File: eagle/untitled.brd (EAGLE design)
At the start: 100 x 80 mm, 11 parts, among them U1 ESP-WROOM-32

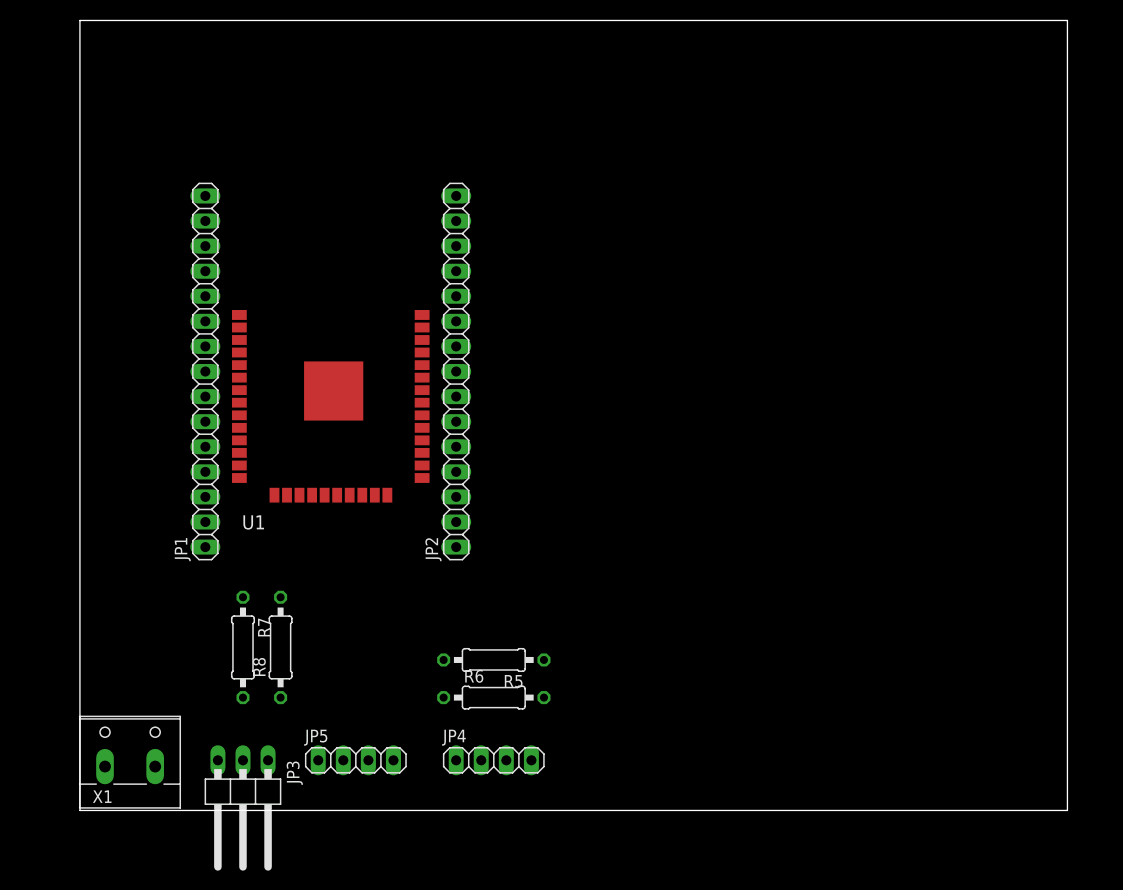
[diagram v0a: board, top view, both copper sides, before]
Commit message: #Eagle - Change Arduino symbol
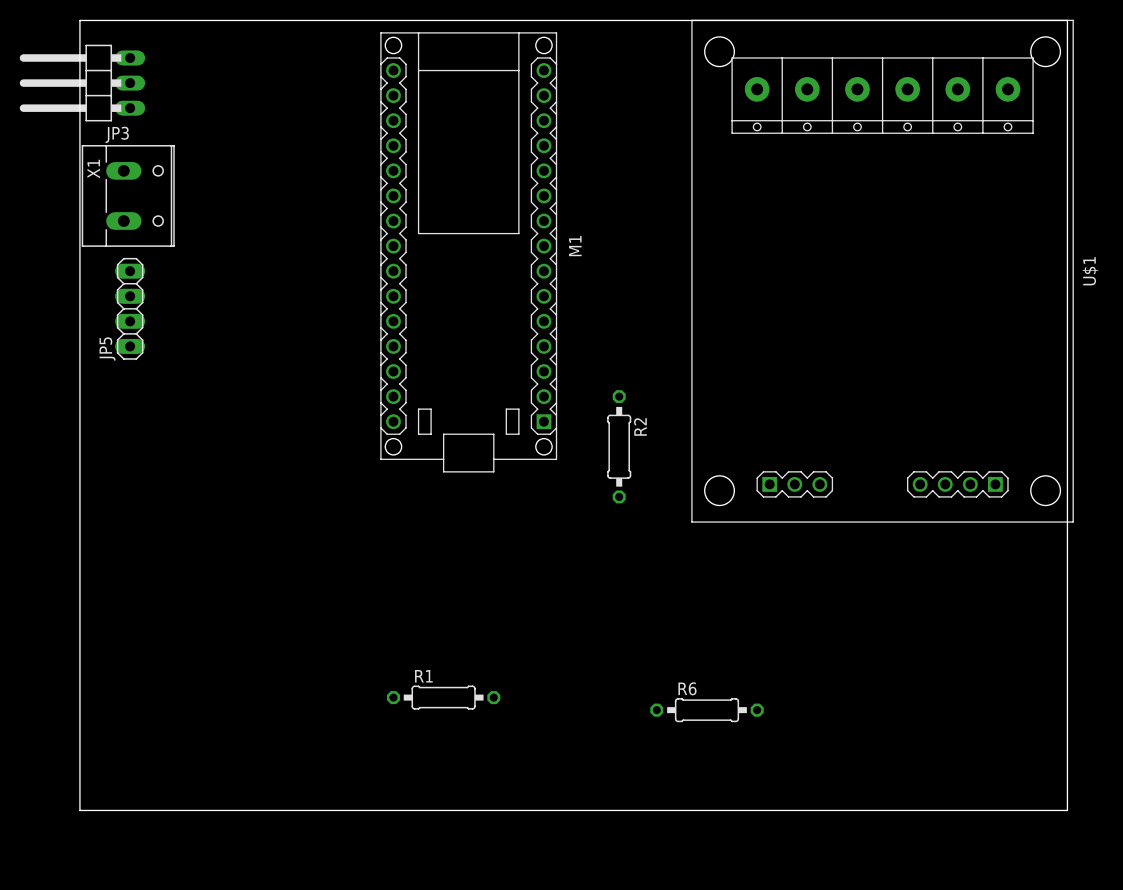
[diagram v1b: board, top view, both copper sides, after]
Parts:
- removed JP1, JP2: (no value), pinhead:1X15
- removed JP4: Relay, pinhead:1X04
- removed R5, R7, R8: (no value), resistor:0207/10
- removed U1: ESP-WROOM-32, esp32:ESP-WROOM-32
- added M1: ARDUINO-NANO-3.0, diy-modules:ARDUINO-NANO-3.0
- added R1, R2: 10k, resistor:0207/10
- added U$1: RELAY-2-SRD#RC, diy-modules:RELAY-2-SRD#RC
- R6: value (none) -> 10k
- moved JP3 74.0 mm to (1.27, 73.7), turned to 90 degrees
- moved X1 57.1 mm to (5.08, 62.2), turned to 270 degrees
- moved JP5 51.1 mm to (5.08, 50.8), turned to 90 degrees
- moved R6 21.6 mm to (63.5, 10.2)
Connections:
- removed net N$6: JP5.1, U1.11
- removed net N$8: JP5.2, U1.10
- net GND: now also JP3.3, M1.J1.14, M1.J2.14, R1.1, U$1.J1.4, U$1.J2.3, U$1.P1.3, U$1.P1.6; no longer JP2.1, JP3.1, JP4.4, R6.1, R8.1, U1.1, U1.15, U1.38
- net N$1: now also JP3.2, M1.J2.7, R6.1; no longer R7.1, R8.2, U1.6
- net N$2: now also M1.J1.2, R1.2, R2.1; no longer R5.1, R6.2, U1.7
- net N$3: now also M1.J1.8, U$1.J1.2; no longer JP1.5, JP4.2, U1.33
- net N$4: now also M1.J1.9, U$1.J1.3; no longer JP1.6, JP4.3, U1.GND
- net N$5: now also U$1.J2.1, U$1.J2.2; no longer JP3.2, R7.2
- net VCC: now also JP3.1, M1.J1.15, M1.J2.15, R2.2, R6.2, U$1.J1.1, U$1.P1.1, U$1.P1.4; no longer JP2.2, JP3.3, JP4.1, R5.2, U1.2
